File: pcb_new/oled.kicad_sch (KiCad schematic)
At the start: 29 parts, among them J10 3-2328724-1, U8 TPS6734ID

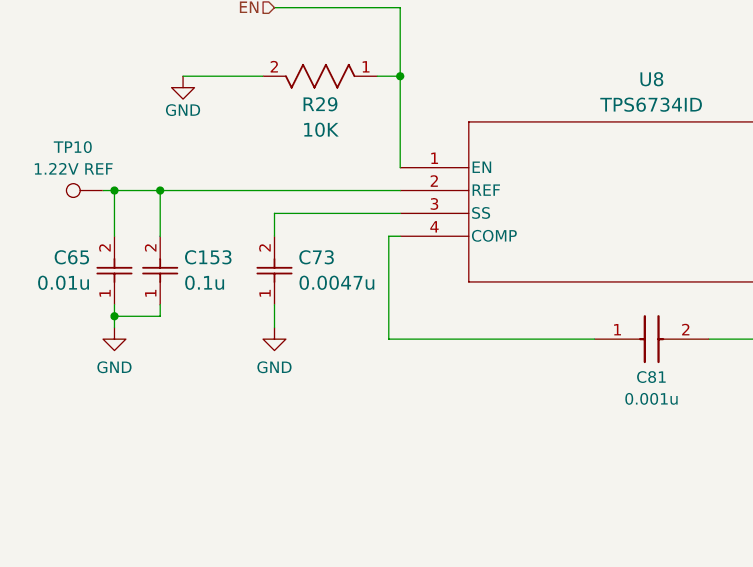
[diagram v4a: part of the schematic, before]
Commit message: fix OLED SS capacitor value (closes #71)
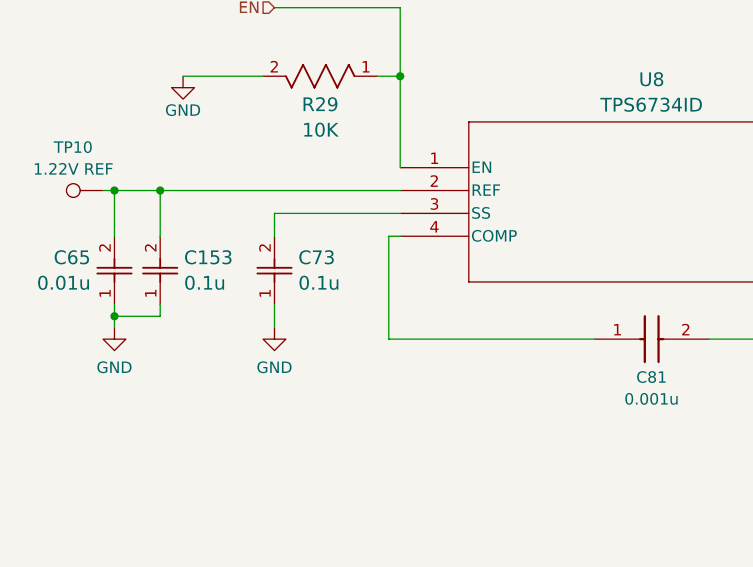
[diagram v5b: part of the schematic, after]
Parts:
- removed C73: 0.0047u, OroLink:CAP_GCM155_MUR, symbol OroLink:GCM155L81H472KA37D
- added C73: 0.1u, OroLink:CAP_MSAS1L-3_TAY, symbol OroLink:MSAST1L3YB5104KFNA01
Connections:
- net GND: now also C73.1
- net at U8.3 (SS): now also C73.2
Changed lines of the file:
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@@
+	)
+	(symbol
+		(lib_id "OroLink:MSAST1L3YB5104KFNA01")
+		(at 44.45 121.92 90)
+		(unit 1)
+		(exclude_from_sim no)
+		(in_bom yes)
+		(on_board yes)
+		(dnp no)
+		(fields_autoplaced yes)
+		(property "Reference" "C73"
+			(at 47.0916 116.6935 90)
+			(effects
+				(font
+					(size 1.524 1.524)
+				)
+				(justify right)
+			)
+		)
+		(property "Value" "0.1u"
+			(at 47.0916 119.5264 90)
+			(effects
+				(font
+					(size 1.524 1.524)
+				)
+				(justify right)
+			)
+		)
+		(property "Footprint" "OroLink:CAP_MSAS1L-3_TAY"
+			(at 44.45 121.92 0)
+			(effects
+				(font
+					(size 1.27 1.27)
+					(italic yes)
+				)
+				(hide yes)
+			)
+		)
+		(property "Datasheet" "https://www.mouser.de/datasheet/2/396/Tayio_Yuden_1102023_MS_mlcc_all_e-3081579.pdf"
+			(at 44.45 121.92 0)
+			(effects
+				(font
+					(size 1.27 1.27)
+					(italic yes)
+				)
+				(hide yes)
+			)
+		)
+		(property "Description" "Multilayer Ceramic Capacitor, 0.1 uF, 25 V, ± 10%, X5R, 0402 [1005 Metric] - T&R"
+			(at 44.45 121.92 0)
+			(effects
+				(font
+					(size 1.27 1.27)
+				)
+				(hide yes)
+			)
+		)
+		(property "Mfr. Name" "Taiyo Yuden"
+			(at 47.45 121.92 0)
+			(effects
+				(font
+					(size 1.27 1.27)
+					(italic yes)
+				)
+				(hide yes)
+			)
+		)
+		(property "Mfr. Number" "MSAST1L3YB5104KFNA01"
+			(at 47.45 121.92 0)
+			(effects
+				(font
+					(size 1.27 1.27)
+					(italic yes)
+				)
+				(hide yes)
+			)
+		)
+		(property "Mouser URL" "https://www.mouser.de/ProductDetail/TAIYO-YUDEN/MSAST1L3YB5104KFNA01?qs=tlsG%2FOw5FFhBwK%252BMwEZpCA%3D%3D"
+			(at 47.45 121.92 0)
+			(effects
+				(font
+					(size 1.27 1.27)
+					(italic yes)
+				)
+				(hide yes)
+			)
+		)
+		(property "Description_1" "Multilayer Ceramic Capacitor, 0.1 uF, 25 V, ± 10%, X5R, 0402 [1005 Metric] - T&R"
+			(at 47.45 121.92 0)
+			(effects
+				(font
+					(size 1.27 1.27)
+					(italic yes)
+				)
+				(hide yes)
+			)
+		)
+		(property "Arrow ID" "MSAST1L3YB5104KFNA01"
+			(at 47.45 121.92 0)
+			(effects
+				(font
+					(size 1.27 1.27)
+					(italic yes)
+				)
+				(hide yes)
+			)
+		)
+		(property "DigiKey ID" "587-MSAST1L3YB5104KFNA01CT-ND"
+			(at 47.45 121.92 0)
+			(effects
+				(font
+					(size 1.27 1.27)
+					(italic yes)
+				)
+				(hide yes)
+			)
+		)
+		(property "Mouser ID" "963-MSAST1L3YB5104KF"
+			(at 47.45 121.92 0)
+			(effects
+				(font
+					(size 1.27 1.27)
+					(italic yes)
+				)
+				(hide yes)
+			)
+		)
+		(pin "1"
+		)
+		(pin "2"
+		)
+		(instances
+			(project "link"
+				(path "/b8dafc19-6de0-4c8f-9903-23372e5103df/222205f2-0600-4315-a593-542b8c55a37e"
+					(reference "C73")
+					(unit 1)
+				)
+			)
+		)
 	)
 	(symbol
@@
 					(unit 1)
 				)
-			)
-		)
-	)
-	(symbol
-		(lib_id "OroLink:GCM155L81H472KA37D")
-		(at 44.45 121.92 90)
-		(unit 1)
-		(exclude_from_sim no)
-		(in_bom yes)
-		(on_board yes)
-		(dnp no)
-		(fields_autoplaced yes)
-		(property "Reference" "C73"
-			(at 47.0916 116.6935 90)
-			(effects
-				(font
-					(size 1.524 1.524)
-				)
-				(justify right)
-			)
-		)
-		(property "Value" "0.0047u"
-			(at 47.0916 119.5264 90)
-			(effects
-				(font
-					(size 1.524 1.524)
-				)
-				(justify right)
-			)
-		)
-		(property "Footprint" "OroLink:CAP_GCM155_MUR"
-			(at 44.45 121.92 0)
-			(effects
-				(font
-					(size 1.27 1.27)
-					(italic yes)
-				)
-				(hide yes)
-			)
-		)
-		(property "Datasheet" "https://www.mouser.de/datasheet/2/281/1/GCM155L81H472KA37_01A-3142077.pdf"
-			(at 44.45 121.92 0)
-			(effects
-				(font
-					(size 1.27 1.27)
-					(italic yes)
-				)
-				(hide yes)
-			)
-		)
-		(property "Description" "CERAMIC CAPACITOR 0402 ceramic capacitor -40/+15% ppm/C 10% 4.7nF"
-			(at 44.45 121.92 0)
-			(effects
-				(font
-					(size 1.27 1.27)
-				)
-				(hide yes)
-			)
-		)
-		(property "Mfr. Name" "Murata"
-			(at 47.45 121.92 0)
-			(effects
-				(font
-					(size 1.27 1.27)
-					(italic yes)
-				)
-				(hide yes)
-			)
-		)
-		(property "Arrow ID" "GCM155L81H472KA37D"
-			(at 47.45 121.92 0)
-			(effects
-				(font
-					(size 1.27 1.27)
-					(italic yes)
-				)
-				(hide yes)
-			)
-		)
-		(property "Mouser ID" "81-GCM155L81H472KA7D"
-			(at 47.45 121.92 0)
-			(effects
-				(font
-					(size 1.27 1.27)
-					(italic yes)
-				)
-				(hide yes)
-			)
-		)
-		(property "DigiKey ID" "490-GCM155L81H472KA37DCT-ND"
-			(at 47.45 121.92 0)
-			(effects
-				(font
-					(size 1.27 1.27)
-					(italic yes)
-				)
-				(hide yes)
-			)
-		)
-		(property "Description_1" "CERAMIC CAPACITOR 0402 ceramic capacitor -40/+15% ppm/C 10% 4.7nF"
-			(at 47.45 121.92 0)
-			(effects
-				(font
-					(size 1.27 1.27)
-					(italic yes)
-				)
-				(hide yes)
-			)
-		)
-		(property "Mfr. Number" "GCM155L81H472KA37D"
-			(at 47.45 121.92 0)
-			(effects
-				(font
-					(size 1.27 1.27)
-					(italic yes)
-				)
-				(hide yes)
-			)
-		)
-		(property "Mouser URL" "https://www.mouser.de/ProductDetail/Murata-Electronics/GCM155L81H472KA37D?qs=ui%252B2d9lVEI75WI3HYc0yTw%3D%3D&utm_source=octopart&utm_medium=aggregator&utm_campaign=81-GCM155L81H472KA7D&utm_content=Murata"
-			(at 47.45 121.92 0)
-			(effects
-				(font
-					(size 1.27 1.27)
-					(italic yes)
-				)
-				(hide yes)
-			)
-		)
-		(pin "2"
-		)
-		(pin "1"
-		)
-		(instances
-			(project ""
-				(path "/b8dafc19-6de0-4c8f-9903-23372e5103df/222205f2-0600-4315-a593-542b8c55a37e"
-					(reference "C73")
-					(unit 1)
-				)
